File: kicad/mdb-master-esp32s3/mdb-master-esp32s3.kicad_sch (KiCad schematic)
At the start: 32 parts, among them J1 MDB_Connector, J2 Barrel_Jack, J3 USB_C_Receptacle_USB2.0_16P, J4 Conn_02x11_Odd_Even, Q1 BC807, SW1 SW_Push, U1 ESP32-S3R8, U2 AMS1117-3.3, Y1 40000hz

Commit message: Refacting PCB
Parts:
- removed TP1: TestPoint, TestPoint:TestPoint_Pad_D1.0mm, symbol Connector:TestPoint
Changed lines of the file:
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@@
-		(color 0 0 0 0)
-	)
-	(junction
-		(at 90.17 97.79)
-		(diameter 0)
 		(color 0 0 0 0)
 	)
@@
 	(wire
 		(pts
-			(xy 81.28 97.79) (xy 90.17 97.79)
+			(xy 81.28 97.79) (xy 109.22 97.79)
 		)
 		(stroke
@@
 		(pts
 			(xy 181.61 130.81) (xy 184.15 130.81)
-		)
-		(stroke
-			(width 0)
-			(type default)
-		)
-	)
-	(wire
-		(pts
-			(xy 90.17 97.79) (xy 109.22 97.79)
 		)
 		(stroke
@@
 					(unit 1)
 				)
-			)
-		)
-	)
-	(symbol
-		(lib_id "Connector:TestPoint")
-		(at 90.17 97.79 0)
-		(unit 1)
-		(exclude_from_sim no)
-		(in_bom yes)
-		(on_board yes)
-		(dnp no)
-		(fields_autoplaced yes)
-		(property "Reference" "TP1"
-			(at 92.71 93.2179 0)
-			(effects
-				(font
-					(size 1.27 1.27)
-				)
-				(justify left)
-			)
-		)
-		(property "Value" "TestPoint"
-			(at 92.71 95.7579 0)
-			(effects
-				(font
-					(size 1.27 1.27)
-				)
-				(justify left)
-			)
-		)
-		(property "Footprint" "TestPoint:TestPoint_Pad_D1.0mm"
-			(at 95.25 97.79 0)
-			(effects
-				(font
-					(size 1.27 1.27)
-				)
-				(hide yes)
-			)
-		)
-		(property "Datasheet" "~"
-			(at 95.25 97.79 0)
-			(effects
-				(font
-					(size 1.27 1.27)
-				)
-				(hide yes)
-			)
-		)
-		(property "Description" "test point"
-			(at 90.17 97.79 0)
-			(effects
-				(font
-					(size 1.27 1.27)
-				)
-				(hide yes)
-			)
-		)
-		(pin "1"
-		)
-		(instances
-			(project ""
-				(path "/1a9a25ce-6784-46e5-b680-57f383f3a43d"
-					(reference "TP1")
-					(unit 1)
-				)

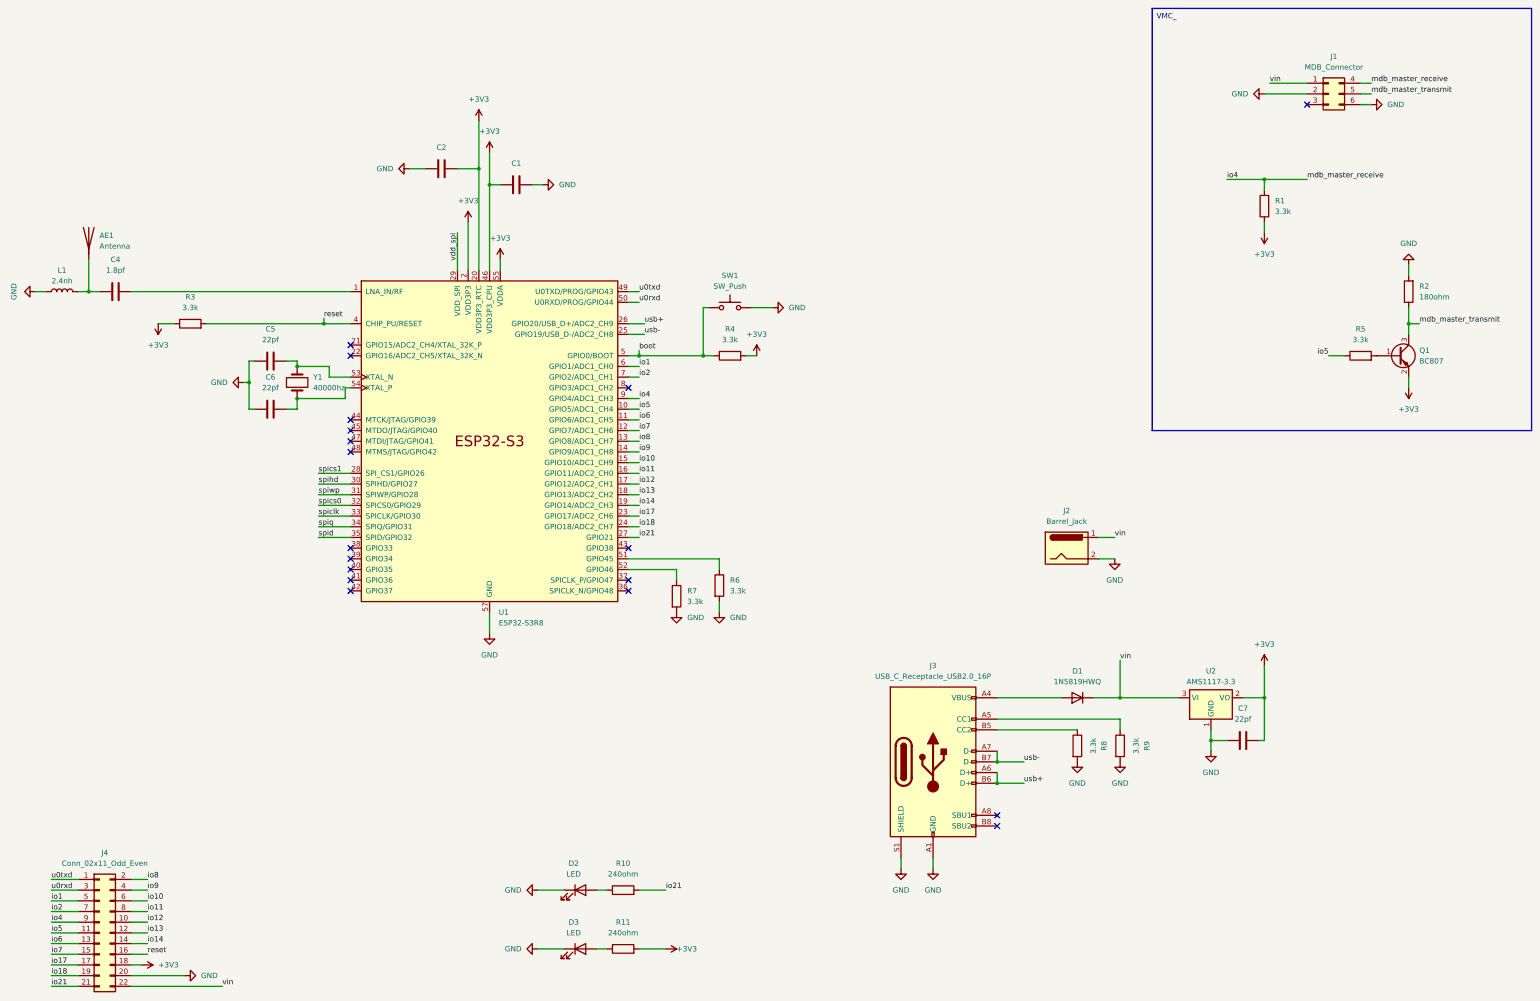
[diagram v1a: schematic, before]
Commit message: Refacting kicad layout
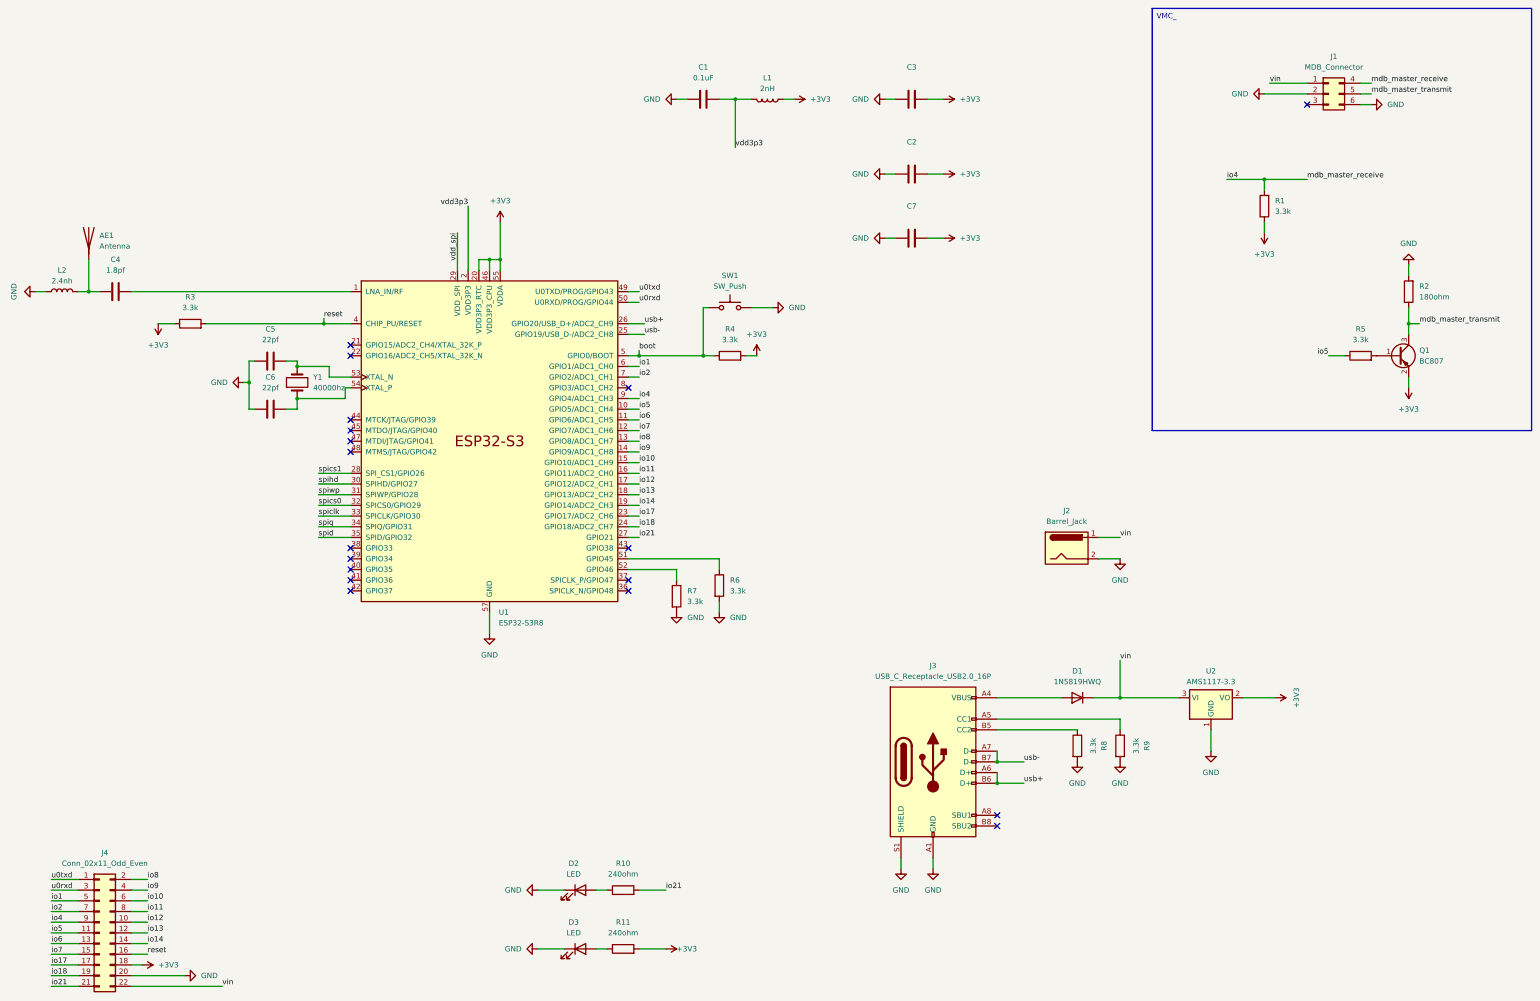
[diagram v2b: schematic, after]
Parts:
- added C3: 10uF, Capacitor_SMD:C_0603_1608Metric, symbol Device:C
- added L1: 2nH, Inductor_SMD:L_0603_1608Metric, symbol Device:L
- C1: value C -> 0.1uF
- C2: value C -> 1uF
- C7: value 22pf -> 1uF
- U1: footprint Package_DFN_QFN:QFN-56-1EP_7x7mm_P0.4mm_EP5.6x5.6mm -> Package_DFN_QFN:QFN-56-1EP_7x7mm_P0.4mm_EP4x4mm
- renumbered L1 to L2
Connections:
- net +3V3: now also C2.2, C3.2, L1.1; no longer C1.2, C2.1, U1.2 (VDD3P3), U1.3 (VDD3P3)
- net GND: now also C1.2, C2.1, C3.1; no longer C1.1, C2.2
- new net VDD3P3: C1.1, L1.2, U1.2 (VDD3P3), U1.3 (VDD3P3)
